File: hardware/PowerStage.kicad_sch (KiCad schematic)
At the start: 0 parts

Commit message: Populate Power Stage sheet
- 3x half-bridge (NTMFS006N08MC x6), driven by DRV8323 GHx/GLx/SHx
- 3x Kelvin current shunts (2 mOhm 1W) - found and worked around
  another vendor-symbol quirk: the shunt is a real 4-terminal Kelvin
  part with force+sense pads sharing pin numbers, needing a second
  label pass per shunt (same class of issue as DRV8323's WP#/SWEN,
  but this one is intentional/correct part modeling, not a bug)
- TMP235 temperature sensor near the FET cluster
- 3x phase output screw terminals
- Hot-loop + DC-bus bulk decoupling
- LAYOUT notes for Kelvin sensing and hot-loop caps per design rules

Co-Authored-By: Claude Sonnet 5 <noreply@anthropic.com>
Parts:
- added C29, C30: Hot-loop bulk, symbol METUPowerLab_Capacitors_Ceramics_SurfaceMounts:10 µF 75V
- added C31, C32: DC bus bulk, METUPowerLab_Capacitors_AluminumPolymers_ThroughHoles:8.00x13.50mm, symbol METUPowerLab_Capacitors_AluminumPolymers_ThroughHoles:100 µF
- added J5: PHASE_A, METUPowerLab_Connectors_ScrewTerminals:7770, symbol METUPowerLab_Connectors_ScrewTerminals:7770
- added J6: PHASE_B, METUPowerLab_Connectors_ScrewTerminals:7770, symbol METUPowerLab_Connectors_ScrewTerminals:7770
- added J7: PHASE_C, METUPowerLab_Connectors_ScrewTerminals:7770, symbol METUPowerLab_Connectors_ScrewTerminals:7770
- added Q2: Phase A high-side, METUPowerLab_Transistors_MOSFETs:8-PowerTDFN(5x6mm), symbol METUPowerLab_Transistors_MOSFETs:NTMFS006N08MC
- added Q3: Phase A low-side, METUPowerLab_Transistors_MOSFETs:8-PowerTDFN(5x6mm), symbol METUPowerLab_Transistors_MOSFETs:NTMFS006N08MC
- added Q4: Phase B high-side, METUPowerLab_Transistors_MOSFETs:8-PowerTDFN(5x6mm), symbol METUPowerLab_Transistors_MOSFETs:NTMFS006N08MC
- added Q5: Phase B low-side, METUPowerLab_Transistors_MOSFETs:8-PowerTDFN(5x6mm), symbol METUPowerLab_Transistors_MOSFETs:NTMFS006N08MC
- added Q6: Phase C high-side, METUPowerLab_Transistors_MOSFETs:8-PowerTDFN(5x6mm), symbol METUPowerLab_Transistors_MOSFETs:NTMFS006N08MC
- added Q7: Phase C low-side, METUPowerLab_Transistors_MOSFETs:8-PowerTDFN(5x6mm), symbol METUPowerLab_Transistors_MOSFETs:NTMFS006N08MC
- added RS1: Phase A shunt, symbol METUPowerLab_Resistors_ShuntResistors:2 mOhm 1Watt
- added RS2: Phase B shunt, symbol METUPowerLab_Resistors_ShuntResistors:2 mOhm 1Watt
- added RS3: Phase C shunt, symbol METUPowerLab_Resistors_ShuntResistors:2 mOhm 1Watt
- added U8: TMP235A4DCKR, METUPowerLab_Sensors_Temperature:SC-70-5, symbol METUPowerLab_Sensors_Temperature:TMP235A4DCKR
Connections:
- new net +3V3_MCU: U8.4 (VDD)
- new net +VBUS_PROT: C29.1, C30.1, C31.1, C32.1, Q2.3 (D), Q4.3 (D), Q6.3 (D)
- new net GHA: Q2.2 (G)
- new net GHB: Q4.2 (G)
- new net GHC: Q6.2 (G)
- new net GLA: Q3.2 (G)
- new net GLB: Q5.2 (G)
- new net GLC: Q7.2 (G)
- new net GND: C29.2, C30.2, C31.2, C32.2, RS1.2, RS2.2, RS3.2, U8.2 (GND)
- new net SHA: J5.1, Q2.1 (S), Q3.3 (D)
- new net SHB: J6.1, Q4.1 (S), Q5.3 (D)
- new net SHC: J7.1, Q6.1 (S), Q7.3 (D)
- new net SPA: Q3.1 (S), RS1.1
- new net SPB: Q5.1 (S), RS2.1
- new net SPC: Q7.1 (S), RS3.1
- new net TEMP_SENSE: U8.3 (VOUT)
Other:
- note added: "LAYOUT: Kelvin connection - route SPx/SNx as dedicated sense traces directly to each shunt pad, no shared copper with the power path LAYOUT: C29/C30/C31/C32 directly across VM/PGND at the half-bridges (hot loop, keep loop area minimal) LAYOUT: Q2-Q7 phase current per §3.3 (this design's ~5-10A target) - size PHASE_A/B/C and +VBUS_PROT copper accordingly LAYOUT: Place U8 (TMP235) thermally close t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"

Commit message: Populate Current Sensing + Communication sheets; schematic complete
Current Sensing:
- DC-bus shunt (5 mOhm, in series after the eFuse - required renaming
  the eFuse OUT net to +VBUS_EFUSE_OUT so the shunt sits properly
  in-line ahead of +VBUS_PROT)
- INA240 total-bus current sense, unidirectional config, -> MCU ADC

Communication:
- SN65HVD230 CAN transceiver (3.3V native) on ESP32 TWAI pins
- Per-line TVS (SP0115-01UTG) on CANH/CANL
- 4-pin bus connector (CANH/CANL/GND/+VBUS_PROT)

Whole-hierarchy ERC (all 6 sheets + root) now down to 3 residual
errors, all the same benign/expected 'two power_out pins on one net'
pattern (datasheet-recommended parallel pins, or a PWR_FLAG sharing
a net with a real driver) - fully explained in ARCHITECTURE.md, which
now also documents the found-and-worked-around vendor library defects
(eFuse pin-20 duplication, TMP235 VOUT mistyped as input) and confirms
the shunt 'duplicate pins' are correct 4-terminal Kelvin modeling, not
a bug.

All 6 hierarchical sheets are now fully wired end to end:
Power Supply -> MCU Core -> Gate Drive -> Power Stage, with Current
Sensing and Communication cross-wired throughout.

Co-Authored-By: Claude Sonnet 5 <noreply@anthropic.com>
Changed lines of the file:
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@@
+		)
+	)
+	(symbol
+		(lib_id "power:PWR_FLAG")
+		(at 100.33 77.47 0)
+		(unit 1)
+		(body_style 1)
+		(exclude_from_sim no)
+		(in_bom yes)
+		(on_board yes)
+		(in_pos_files yes)
+		(dnp no)
+		(property "Reference" "#FLG7"
+			(at 100.33 79.375 0)
+			(hide yes)
+			(show_name no)
+			(do_not_autoplace no)
+			(effects
+				(font
+					(size 1.27 1.27)
+				)
+			)
+		)
+		(property "Value" "PWR_FLAG"
+			(at 100.33 81.28 0)
+			(show_name no)
+			(do_not_autoplace no)
+			(effects
+				(font
+					(size 1.27 1.27)
+				)
+			)
+		)
+		(property "Footprint" ""
+			(at 100.33 77.47 0)
+			(hide yes)
+			(show_name no)
+			(do_not_autoplace no)
+			(effects
+				(font
+					(size 1.27 1.27)
+				)
+			)
+		)
+		(property "Datasheet" ""
+			(at 100.33 77.47 0)
+			(hide yes)
+			(show_name no)
+			(do_not_autoplace no)
+			(effects
+				(font
+					(size 1.27 1.27)
+				)
+			)
+		)
+		(property "Description" "Special symbol for telling ERC where power comes from"
+			(at 100.33 77.47 0)
+			(hide yes)
+			(show_name no)
+			(do_not_autoplace no)
+			(effects
+				(font
+					(size 1.27 1.27)
+				)
+			)
+		)
+		(pin "1"
+		)
+		(instances
+			(project "ESC3Phase"
+				(path "/ca73365a-f995-45d9-ac55-18c98119c2ec"
+					(reference "#FLG7")
+					(unit 1)
+				)
+			)
+		)
+	)
+	(global_label "TEMP_SENSE"
+		(at 100.33 77.47 270)
+		(effects
+			(font
+				(size 1.27 1.27)
+			)
+			(justify right)
 		)
 	)

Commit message: PCB layout: board outline, mounting holes, footprint placement, copper pours, phase-output routing
- 100x115mm 2-layer board, 4x M3 mounting holes, design rules per PowerLab spec
- All 55 schematic components synced to board with real footprints
- Auto-placed via force-directed placement with locked connector/MCU anchors
- GND pour (both layers) + localized pours for VIN_RAW/+VBUS/+VBUS_EFUSE_OUT/+VBUS_PROT/+5V_LOGIC
- Routed the 3 critical phase-output traces (SHA/SHB/SHC, 2mm wide)
- Documented full PCB status in ARCHITECTURE.md: NOT yet fab-ready (732 DRC
  violations, 21 courtyard overlaps, ~50 signal nets still unrouted since
  Freerouting is unavailable in this environment)

Co-Authored-By: Claude Sonnet 5 <noreply@anthropic.com>
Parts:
- C29, C30: footprint (none) -> METUPowerLab_Capacitors_Ceramics_SurfaceMounts:2220
- RS1, RS2, RS3: footprint (none) -> METUPowerLab_Resistors_ShuntResistors:2010
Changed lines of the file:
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@@
 			)
 		)
-		(property "Footprint" ""
+		(property "Footprint" "METUPowerLab_Resistors_ShuntResistors:2010"
 			(at 59.69 68.58 0)
 			(hide yes)
@@
 			)
 		)
-		(property "Footprint" ""
+		(property "Footprint" "METUPowerLab_Resistors_ShuntResistors:2010"
 			(at 100.33 68.58 0)
 			(hide yes)
@@
 			)
 		)
-		(property "Footprint" ""
+		(property "Footprint" "METUPowerLab_Resistors_ShuntResistors:2010"
 			(at 139.7 68.58 0)
 			(hide yes)
@@
 			)
 		)
-		(property "Footprint" ""
+		(property "Footprint" "METUPowerLab_Capacitors_Ceramics_SurfaceMounts:2220"
 			(at 80.975 29.21 0)
 			(hide yes)
@@
 			)
 		)
-		(property "Footprint" ""
+		(property "Footprint" "METUPowerLab_Capacitors_Ceramics_SurfaceMounts:2220"
 			(at 120.345 29.21 0)
 			(hide yes)

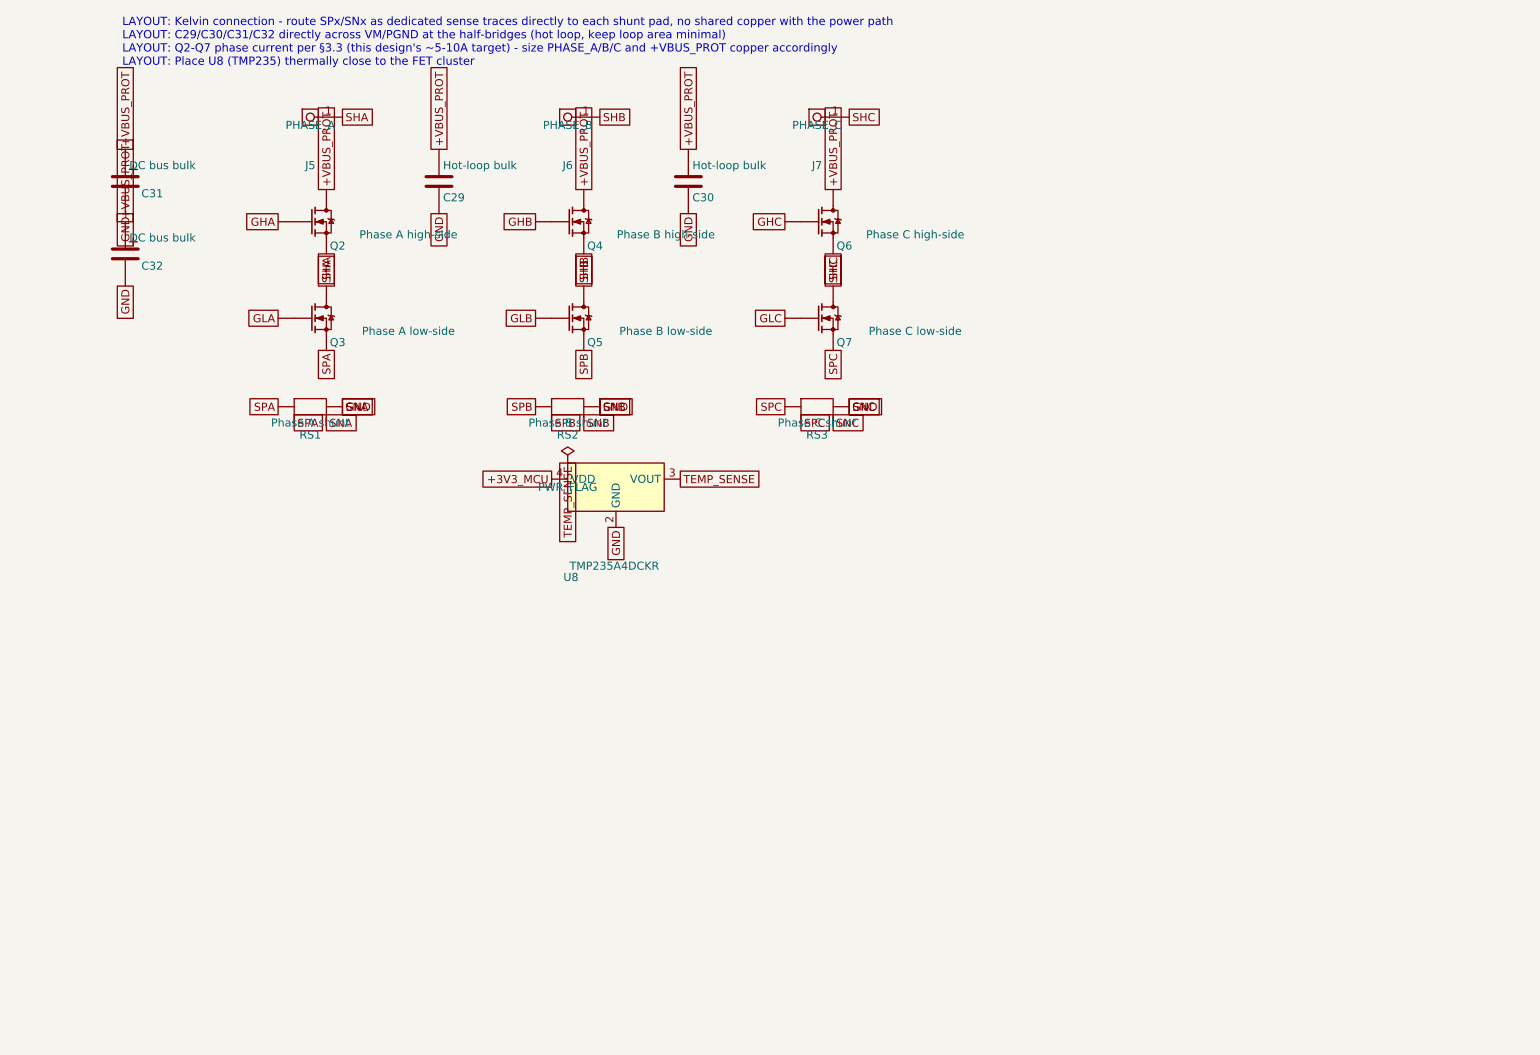
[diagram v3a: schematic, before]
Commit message: Schematic Rev B: full rebuild per METU PowerLab rules
Rev A was withdrawn: labels stuck on pins created real net shorts
(+5V_LOGIC with the 36 V bus, INHA and EFUSE_IMON with GND) and several
circuits contradicted their datasheets.

Rev B: real wires and power symbols on the 2.54 mm grid, hierarchical sheets
(half bridge reused 3x), library values, LAYOUT notes, root page with specs
and block diagram. Circuit fixes: DRV8323 VREF driven, unused buck tied to
GND, INA240A1, LM74700-Q1 reverse polarity, SMBJ36CA, eFuse per datasheet,
direct 3.3 V buck, 4.7 uH/8.1 A inductor, 2512 shunts with net-tie Kelvin,
24 V CAN ESD. kicad-cli ERC: 0 errors; netlist matches intent on all nets.
Old board and project-local library tables removed (board is rebuilt next).

Co-Authored-By: Claude Opus 5.5 <noreply@anthropic.com>
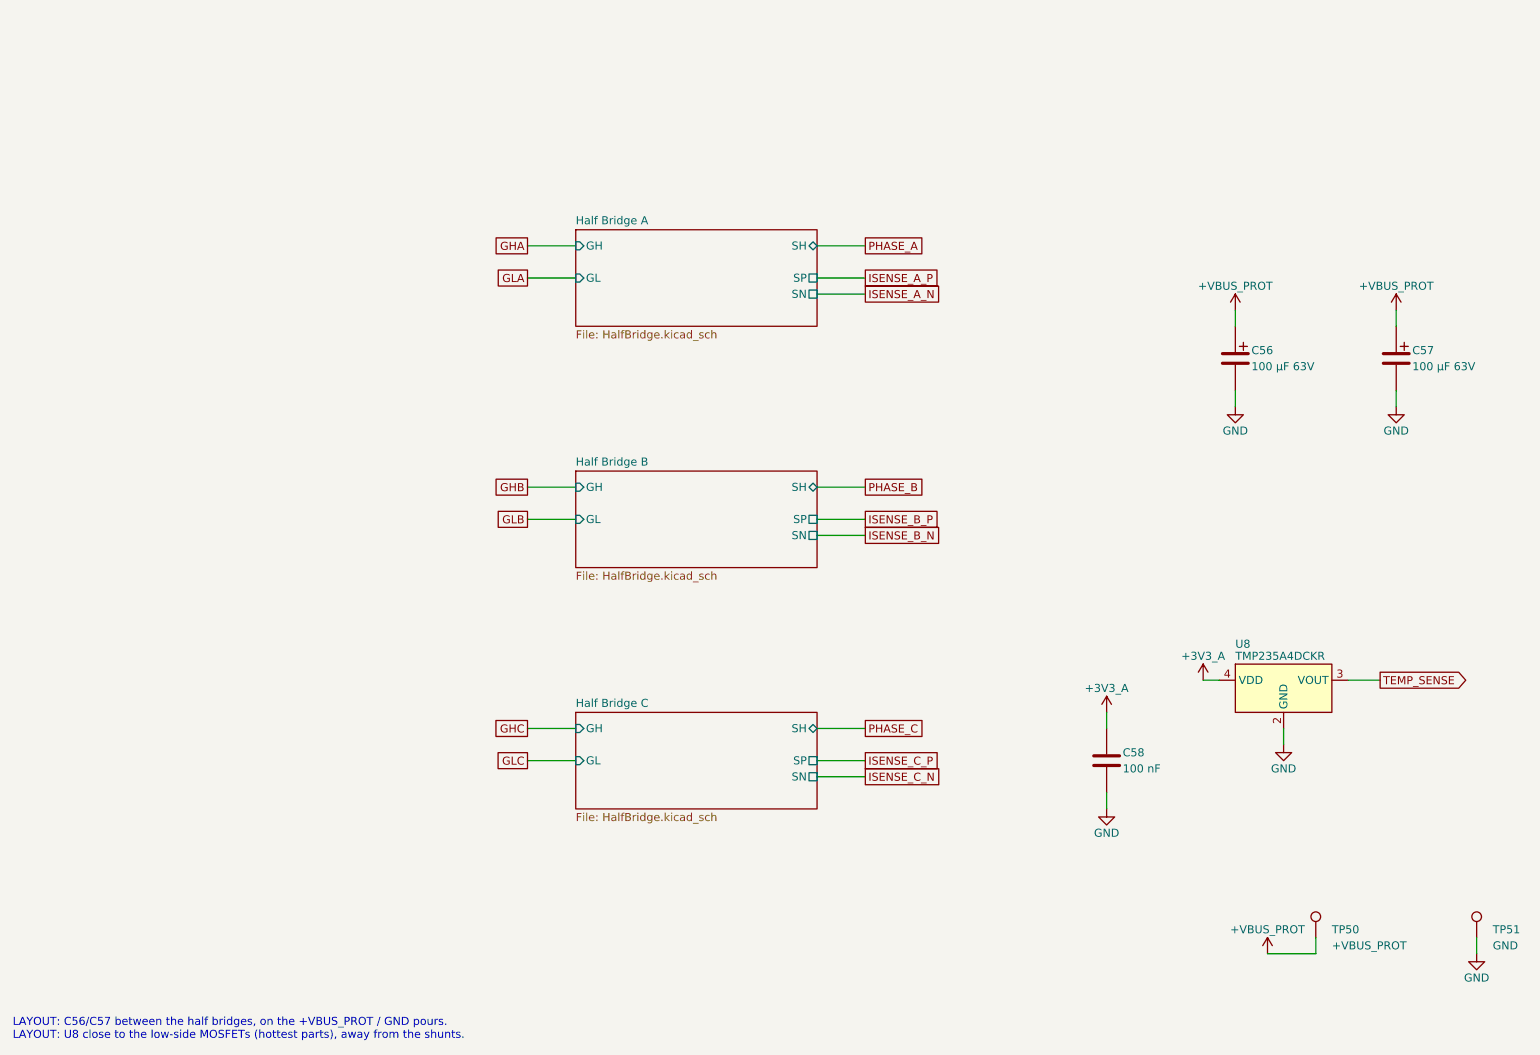
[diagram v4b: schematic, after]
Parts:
- removed C29, C30: Hot-loop bulk, METUPowerLab_Capacitors_Ceramics_SurfaceMounts:2220, symbol METUPowerLab_Capacitors_Ceramics_SurfaceMounts:10 µF 75V
- removed C31, C32: DC bus bulk, METUPowerLab_Capacitors_AluminumPolymers_ThroughHoles:8.00x13.50mm, symbol METUPowerLab_Capacitors_AluminumPolymers_ThroughHoles:100 µF
- removed J5: PHASE_A, METUPowerLab_Connectors_ScrewTerminals:7770, symbol METUPowerLab_Connectors_ScrewTerminals:7770
- removed J6: PHASE_B, METUPowerLab_Connectors_ScrewTerminals:7770, symbol METUPowerLab_Connectors_ScrewTerminals:7770
- removed J7: PHASE_C, METUPowerLab_Connectors_ScrewTerminals:7770, symbol METUPowerLab_Connectors_ScrewTerminals:7770
- removed Q2: Phase A high-side, METUPowerLab_Transistors_MOSFETs:8-PowerTDFN(5x6mm), symbol METUPowerLab_Transistors_MOSFETs:NTMFS006N08MC
- removed Q3: Phase A low-side, METUPowerLab_Transistors_MOSFETs:8-PowerTDFN(5x6mm), symbol METUPowerLab_Transistors_MOSFETs:NTMFS006N08MC
- removed Q4: Phase B high-side, METUPowerLab_Transistors_MOSFETs:8-PowerTDFN(5x6mm), symbol METUPowerLab_Transistors_MOSFETs:NTMFS006N08MC
- removed Q5: Phase B low-side, METUPowerLab_Transistors_MOSFETs:8-PowerTDFN(5x6mm), symbol METUPowerLab_Transistors_MOSFETs:NTMFS006N08MC
- removed Q6: Phase C high-side, METUPowerLab_Transistors_MOSFETs:8-PowerTDFN(5x6mm), symbol METUPowerLab_Transistors_MOSFETs:NTMFS006N08MC
- removed Q7: Phase C low-side, METUPowerLab_Transistors_MOSFETs:8-PowerTDFN(5x6mm), symbol METUPowerLab_Transistors_MOSFETs:NTMFS006N08MC
- removed RS1: Phase A shunt, METUPowerLab_Resistors_ShuntResistors:2010, symbol METUPowerLab_Resistors_ShuntResistors:2 mOhm 1Watt
- removed RS2: Phase B shunt, METUPowerLab_Resistors_ShuntResistors:2010, symbol METUPowerLab_Resistors_ShuntResistors:2 mOhm 1Watt
- removed RS3: Phase C shunt, METUPowerLab_Resistors_ShuntResistors:2010, symbol METUPowerLab_Resistors_ShuntResistors:2 mOhm 1Watt
- added C56, C57: 100 µF 63V, METUPowerLab_Capacitors_AluminumPolymers_ThroughHoles:8.00x13.50mm, symbol METUPowerLab_Capacitors_AluminumPolymers_ThroughHoles:100 µF
- added C58: 100 nF, METUPowerLab_Capacitors_Ceramics_SurfaceMounts:0603_Medium, symbol METUPowerLab_Capacitors_Ceramics_SurfaceMounts:100 nF
- added TP50: +VBUS_PROT, METUPowerLab_TestPoints_SurfaceMounts:Pad_D1.5mm, symbol METUPowerLab_TestPoints_SurfaceMounts:TestPoint_Pad
- added TP51: GND, METUPowerLab_TestPoints_SurfaceMounts:Pad_D1.5mm, symbol METUPowerLab_TestPoints_SurfaceMounts:TestPoint_Pad
- U8: Accuracy (none) -> ±1°C; Digi-Key Number (none) -> 296-50016-1-ND; Manufacturer (none) -> Texas Instruments; Manufacturer Number (none) -> TMP235A4DCKR; Mounting Type (none) -> Surface Mount; Mouser Number (none) -> TMP235A4DCKR; Operating Temperature (none) -> -50°C up to 150°C (TA); Output Type (none) -> Analog Voltage; Package (none) -> SC-70-5; Sensing Temperature Range (none) -> -40°C up to 150°C; Sensor Type (none) -> Analog; Supply Voltage Rating (none) -> 2.3V up to 5.5V
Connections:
- net +VBUS_PROT: now also C56.1, C57.1, TP50.1
- net GND: now also C56.2, C57.2, C58.2, TP51.1
- net +3V3_MCU renamed +3V3_A
- net +3V3_A: now also C58.1
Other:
- added sheet Half Bridge A (HalfBridge.kicad_sch)
- added sheet Half Bridge B (HalfBridge.kicad_sch)
- added sheet Half Bridge C (HalfBridge.kicad_sch)
- note added: "LAYOUT: C56/C57 between the half bridges, on the +VBUS_PROT / GND pours. LAYOUT: U8 close to the low-side MOSFETs (hottest parts), away from the shunts."
- note removed: "LAYOUT: Kelvin connection - route SPx/SNx as dedicated sense traces directly to each shunt pad, no shared copper with the power path LAYOUT: C29/C30/C31/C32 directly across VM/PGND at the half-bridges (hot loop, keep loop area minimal) LAYOUT: Q2-Q7 phase current per §3.3 (this design's ~5-10A target) - size PHASE_A/B/C and +VBUS_PROT copper accordingly LAYOUT: Place U8 (TMP235) thermally close t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"
- title: ${PROJECT_NAME} -> Power Stage
